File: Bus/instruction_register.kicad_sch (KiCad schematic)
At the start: 3 parts, among them J12 Conn_01x07_Pin, J13 Conn_01x08_Pin, J14 Conn_01x08_Pin

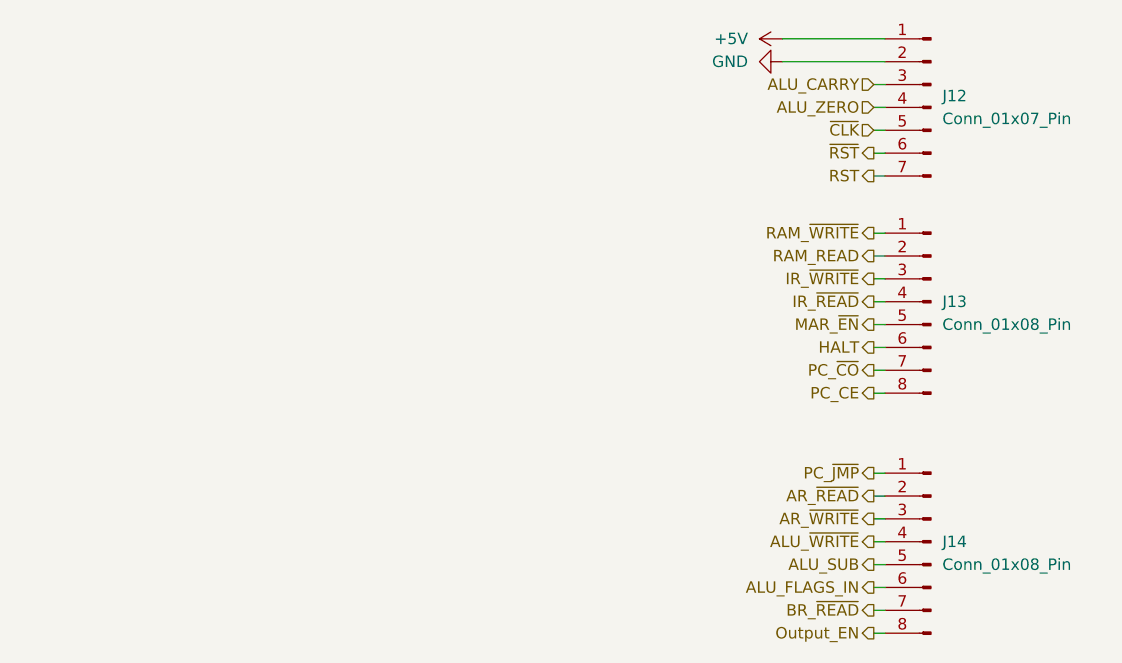
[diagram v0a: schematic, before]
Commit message: Updated bus schmatic pins to match final layouts
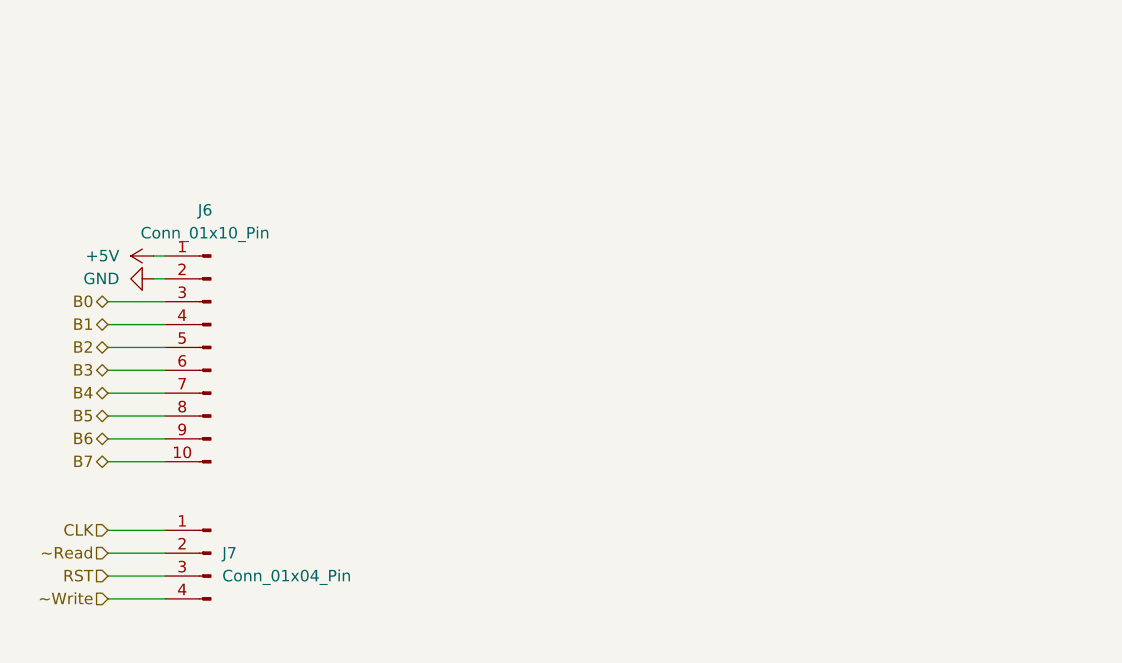
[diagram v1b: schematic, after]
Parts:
- removed J12: Conn_01x07_Pin, Connector_PinHeader_2.54mm:PinHeader_1x07_P2.54mm_Vertical, symbol Connector:Conn_01x07_Pin
- removed J13, J14: Conn_01x08_Pin, Connector_PinHeader_2.54mm:PinHeader_1x08_P2.54mm_Vertical, symbol Connector:Conn_01x08_Pin
- added J6: Conn_01x10_Pin, Connector_PinHeader_2.54mm:PinHeader_1x10_P2.54mm_Vertical, symbol Connector:Conn_01x10_Pin
- added J7: Conn_01x04_Pin, Connector_PinHeader_2.54mm:PinHeader_1x04_P2.54mm_Vertical, symbol Connector:Conn_01x04_Pin
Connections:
- net +5V: now also J6.1 (Pin_1)
- net GND: now also J6.2 (Pin_2)
- net RST: now also J7.3 (Pin_3)
- new net B0: J6.3 (Pin_3)
- new net B1: J6.4 (Pin_4)
- new net B2: J6.5 (Pin_5)
- new net B3: J6.6 (Pin_6)
- new net B4: J6.7 (Pin_7)
- new net B5: J6.8 (Pin_8)
- new net B6: J6.9 (Pin_9)
- new net B7: J6.10 (Pin_10)
- new net CLK: J7.1 (Pin_1)
- new net ~Read: J7.2 (Pin_2)
- new net ~Write: J7.4 (Pin_4)
